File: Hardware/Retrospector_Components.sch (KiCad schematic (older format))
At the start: 143 parts, among them J1 SWD_Header, J2 Eurorack_10_pin_power, J3 Conn_01x08_Male, J4 Conn_01x08_Male, J5 Conn_01x08_Male, J6 Conn_01x08_Male, J7 USB_B_Micro, U1 STM32H743ZITx, U10 LM2675M-5, U11 TL072, U2 IS42S16800F-7TLI, U3 PCM5100APW, U4 AS3364, U5 MCP6004, U6 MCP6004, U7 TL074, U8 LD1117-3.3-4Tab, Y1 8MHz 20pF

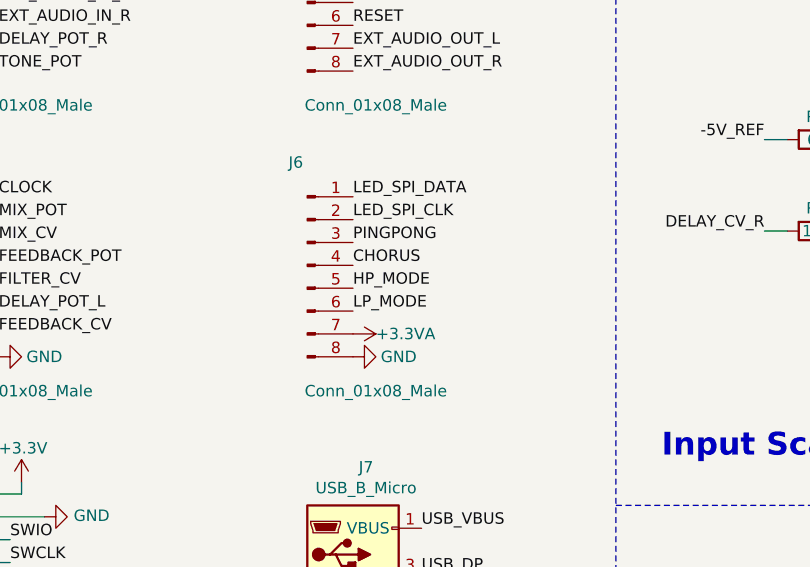
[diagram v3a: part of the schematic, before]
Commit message: Completed routing pass of PCB
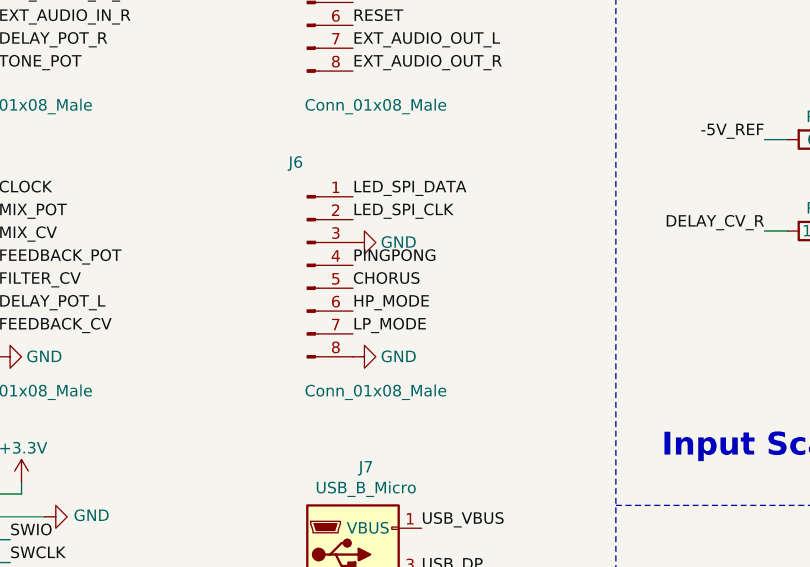
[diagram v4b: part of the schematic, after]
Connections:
- net +3.3VA: no longer J6.7 (Pin_7)
- net CHORUS: now also J6.5 (Pin_5); no longer J6.4 (Pin_4)
- net GND: now also J6.3 (Pin_3)
- net HP_MODE: now also J6.6 (Pin_6); no longer J6.5 (Pin_5)
- net LP_MODE: now also J6.7 (Pin_7); no longer J6.6 (Pin_6)
- net PINGPONG: now also J6.4 (Pin_4); no longer J6.3 (Pin_3)
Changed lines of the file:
@@
 Wire Wire Line
 	14900 1750 14950 1750
-Text Label 7400 7000 0    50   ~ 0
+Text Label 7400 7100 0    50   ~ 0
 CHORUS
 $Comp
@@
 	1    7400 7400
 	0    -1   -1   0
-$EndComp
-$Comp
-L power:+3.3VA #PWR09
-U 1 1 619635CF
-P 7400 7300
-F 0 "#PWR09" H 7400 7150 50  0001 C CNN
-F 1 "+3.3VA" V 7400 7400 50  0000 L CNN
-F 2 "" H 7400 7300 50  0001 C CNN
-F 3 "" H 7400 7300 50  0001 C CNN
-	1    7400 7300
-	0    1    1    0
 $EndComp
 $Comp
@@
 Text Notes 13650 11050 0    50   ~ 0
 FLT: connect to earth for \nhigher latency but less ringing
-Text Label 7400 6900 0    50   ~ 0
+Text Label 7400 7000 0    50   ~ 0
 PINGPONG
+Text Label 7400 7300 0    50   ~ 0
+LP_MODE
 Text Label 7400 7200 0    50   ~ 0
-LP_MODE
-Text Label 7400 7100 0    50   ~ 0
 HP_MODE
 Text Label 7400 6800 0    50   ~ 0
@@
 NoConn ~ 1750 6050
 NoConn ~ 1750 6250
+$Comp
+L power:GND #PWR?
+U 1 1 60F0DC60
+P 7400 6900
+F 0 "#PWR?" H 7400 6650 50  0001 C CNN
+F 1 "GND" V 7400 6700 50  0000 C CNN
+F 2 "" H 7400 6900 50  0001 C CNN
+F 3 "" H 7400 6900 50  0001 C CNN
+	1    7400 6900
+	0    -1   -1   0
+$EndComp
 $EndSCHEMATC

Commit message: Added cycling test mode to RGB LED; Further updates to PCB layout
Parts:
- added C60, C61, C62: 2.2uF, Capacitors_SMD:C_0603_HandSoldering, symbol Device:C_Small
- C47, C48: footprint Capacitors_SMD:C_0805 -> Capacitors_SMD:C_0603_HandSoldering; Part_Number C46653 -> C1588
- C49, C50, C51, C52: footprint Capacitors_SMD:C_0805 -> Capacitors_SMD:C_0603_HandSoldering; Part_Number C1790 -> C14858
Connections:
- net +3.3VA: now also C60.1
- net GND: now also C60.2, C61.2, C62.2; no longer J6.3 (Pin_3)
- net VCC: now also C61.1, C62.1
- net LOCK_BTN: now reaches U1.137 (PB7)
- net LOCK_BTN: now also J6.3 (Pin_3)
- no-connect marks 47 -> 46
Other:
- moved on the sheet: C36, C38, C41, C53, C54, C57, C58, C59, D1, D2, L1, L2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

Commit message: PCB Clean up
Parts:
- added TP13, TP14: TestPoint, Measurement_Points:Measurement_Point_Square-SMD-Pad_Small, symbol Connector:TestPoint
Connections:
- net LOCK_BTN: now also U1.134 (PB4); no longer U1.137 (PB7)
- net I2C1_SCL: now reaches U1.139 (PB8)
- net I2C1_SCL: now also TP14.1
- new net I2C1_SDA: TP13.1, U1.137 (PB7)
- no-connect marks 46 -> 44
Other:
- moved on the sheet: C13, C17, C22, C24, C31, C33, C35, C43, TP1, TP10, TP11, TP12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

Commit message: Further clean up to PCB; started work on using SPI for WS2812 LEDs
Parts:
- renumbered C49 to C1, C14 to C10, C15 to C11, C19 to C12, C46 to C13, C21 to C14, C16 to C15, C20 to C16, C25 to C17, C26 to C18, C37 to C19, C1 to C2, C42 to C20, C44 to C21, C29 to C22, C47 to C23, C6 to C24, C4 to C25, C50 to C26, C30 to C27, C45 to C28, C2 to C29, C5 to C3, C48 to C30, C3 to C31, C51 to C32, C32 to C33, C55 to C34, C52 to C35, C34 to C36, C13 to C37, C17 to C38, C22 to C39, C7 to C4, C24 to C40, C43 to C41, C31 to C42, C39 to C43, C35 to C44, C58 to C45, C60 to C46, C53 to C47, C33 to C48, C18 to C49, C8 to C5, C23 to C50, C27 to C51, C28 to C52, C54 to C53, C57 to C54, C59 to C55, C40 to C57, C38 to C58, C61 to C59, C9 to C6, C62 to C60, C41 to C61, C36 to C62, C10 to C7, C11 to C8, C12 to C9, D3 to D1, D1 to D2, D4 to D3, D2 to D4, J3 to J1, J5 to J2, J4 to J3, J6 to J4, J1 to J5, J7 to J6, J2 to J7, L2 to L1, L1 to L2, R29 to R1, R7 to R10, R41 to R11, R8 to R12, R37 to R14, R39 to R15, R4 to R16, R11 to R17, R9 to R18, R5 to R19, R40 to R2, R18 to R20, R23 to R21, R27 to R22, R35 to R23, R44 to R24, R47 to R25, R24 to R26, R42 to R27, R45 to R28, R21 to R29, R6 to R3, R19 to R30, R48 to R31, R25 to R32, R28 to R33, R46 to R34, R26 to R35, R20 to R36, R10 to R37, R14 to R38, R1 to R39, R12 to R4, R2 to R40, R3 to R41, R15 to R42, R16 to R43, R17 to R44, R43 to R45, R22 to R46, R30 to R5, R34 to R6, R31 to R7, R36 to R8, R38 to R9, U5 to U1, U6 to U1, U8 to U10, U7 to U2, U6 to U3, U5 to U3, U2 to U4, U1 to U5, U11 to U6, U4 to U7, U3 to U8, U10 to U9

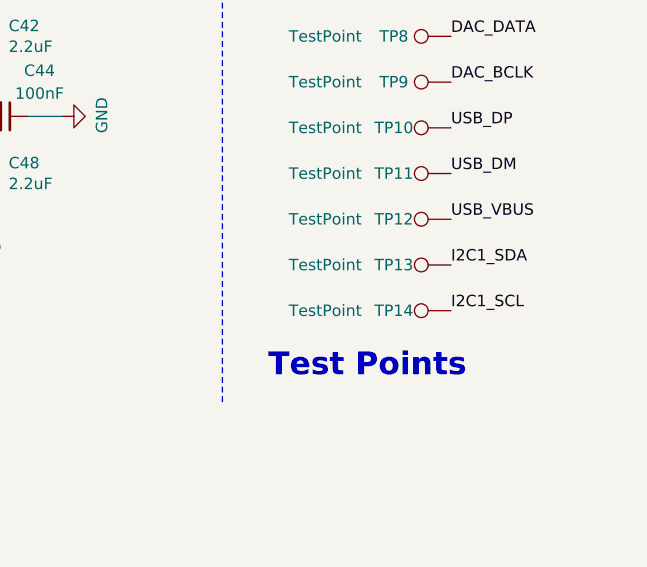
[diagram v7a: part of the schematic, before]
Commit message: Updated controls schematic
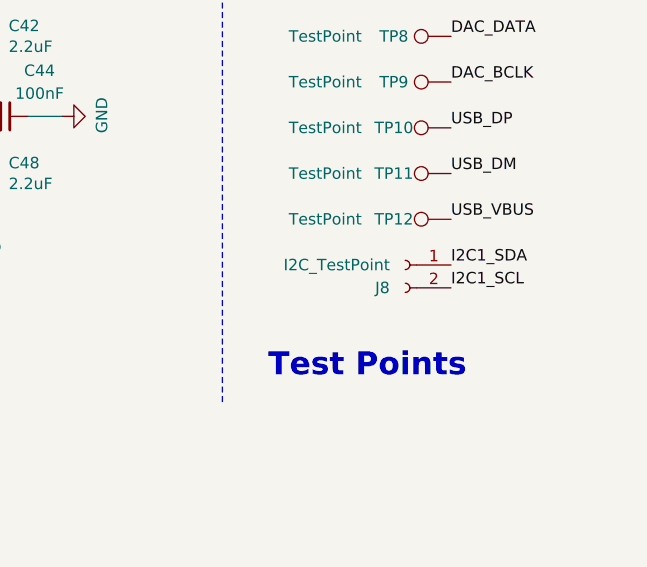
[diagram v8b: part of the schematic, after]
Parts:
- removed TP13, TP14: TestPoint, Measurement_Points:Measurement_Point_Square-SMD-Pad_Small, symbol Connector:TestPoint
- added J8: I2C_TestPoint, Pin_Headers:Pin_Header_Straight_1x02_Pitch2.54mm, symbol Connector:Conn_01x02_Female
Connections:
- net I2C1_SCL: now also J8.2 (Pin_2)
- net I2C1_SDA: now also J8.1 (Pin_1)
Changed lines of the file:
@@
 Text Label 16750 10650 0    50   ~ 0
 I2C1_SDA
-Text Label 16750 10850 0    50   ~ 0
+Text Label 16750 10750 0    50   ~ 0
 I2C1_SCL
 $Comp
-L Connector:TestPoint TP13
-U 1 1 6068145B
-P 16750 10650
-F 0 "TP13" V 16750 10900 50  0000 C CNN
-F 1 "TestPoint" V 16750 11200 50  0000 C CNN
-F 2 "Measurement_Points:Measurement_Point_Square-SMD-Pad_Small" H 16950 10650 50  0001 C CNN
-F 3 "~" H 16950 10650 50  0001 C CNN
-	1    16750 10650
-	0    -1   -1   0
-$EndComp
-$Comp
-L Connector:TestPoint TP14
-U 1 1 606816C0
-P 16750 10850
-F 0 "TP14" V 16750 11100 50  0000 C CNN
-F 1 "TestPoint" V 16750 11400 50  0000 C CNN
-F 2 "Measurement_Points:Measurement_Point_Square-SMD-Pad_Small" H 16950 10850 50  0001 C CNN
-F 3 "~" H 16950 10850 50  0001 C CNN
-	1    16750 10850
-	0    -1   -1   0
+L Connector:Conn_01x02_Female J8
+U 1 1 6065A2AA
+P 16550 10650
+F 0 "J8" H 16650 10550 50  0000 C CNN
+F 1 "I2C_TestPoint" H 16850 10650 50  0000 C CNN
+F 2 "Pin_Headers:Pin_Header_Straight_1x02_Pitch2.54mm" H 16550 10650 50  0001 C CNN
+F 3 "~" H 16550 10650 50  0001 C CNN
+	1    16550 10650
+	-1   0    0    -1
 $EndComp
 $EndSCHEMATC
